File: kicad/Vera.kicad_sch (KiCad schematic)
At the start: 33 parts, among them Q1 AO3400 logic-level N-MOSFET, T1 Wurth 749010012A, T2 Wurth 749010012A, U1 TI AM62A7, U2 Microchip KSZ9477 7-port swit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, U3 TI MSPM0G3507, U4 TI ISOW1044BDFMR (isolated CA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, U5 Infineon SLB9670 TPM 2.0, Y1 25MHz crystal (2-pin symbol s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

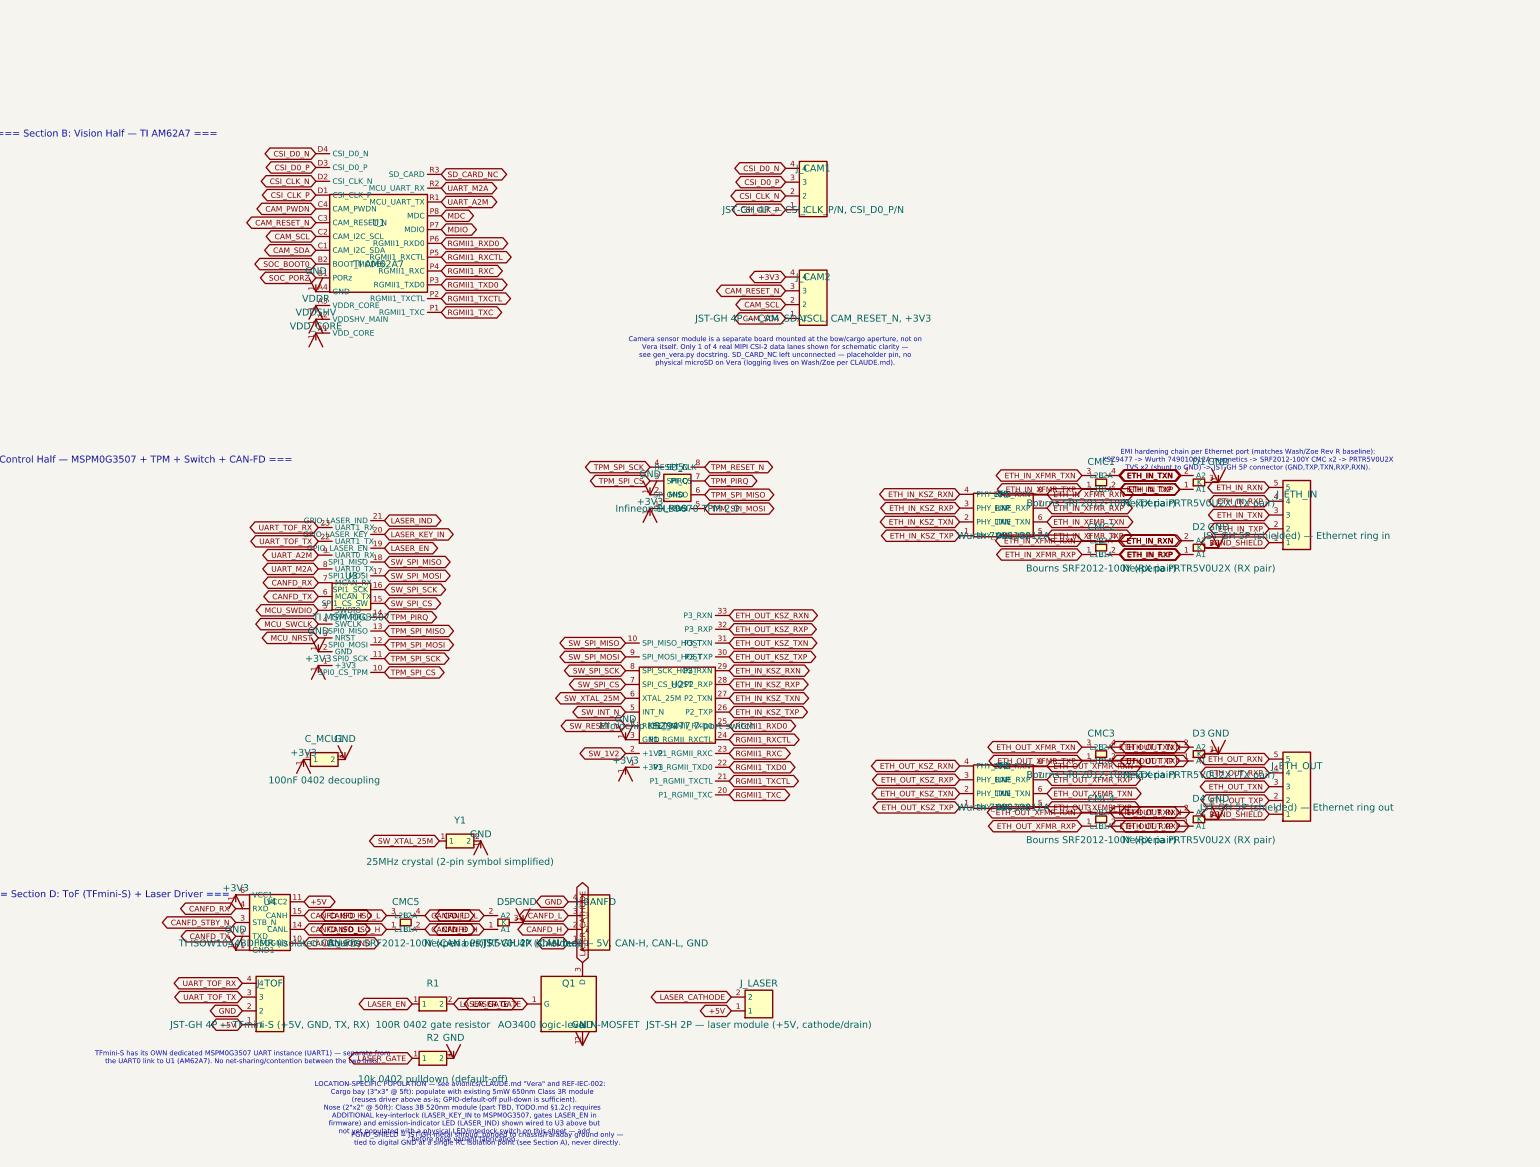
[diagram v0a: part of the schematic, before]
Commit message: Vera: add dual JST/direct-solder sensor interface (camera/ToF/laser) -- schematic
Section 4 of the readiness doc: each nose sensor aperture (camera/ToF/laser) gets
BOTH a JST connector AND a co-located direct-solder land on the SAME nets; populate
one per build (cargo=JST, nose=direct-solder aligned to the sensor mounting plate).

- gen_vera_ds_footprints.py -> Vera.pretty/{DS_Camera_9P,DS_ToF_4P,DS_Laser_2P}.
  kicad_mod: clean-room SMD pad-row lands (1.0mm pitch), pad<->signal order matches
  the JST group. Load in kicad-cli.
- gen_vera.py: adds SolderLand_09P/04P/02P symbols + J_CAM_DS / J_TOF_DS /
  J_LASER_DS instances on the exact JST nets (CSI/I2C/reset/+3V3/GND; +5V/GND/
  TOF_TX/RX; +5V/LASER_CATHODE), grid-aligned, with a populate-one-per-build note.
- fp-lib-table: register the project 'Vera' footprint lib (resolves the DS lands).

ERC 151->154 (+3 = the generic embedded-symbol lib ref that every symbol in this
generated schematic already carries; no connectivity defect -- DS pins join the JST
nets by global label). PCB placement (aligning lands to CAM_POS/TOF_POS/laser CL)
is the next step via a pcbnew script; final XY is a manual mechanical fit.

Co-Authored-By: Claude Opus 4.8 <noreply@anthropic.com>
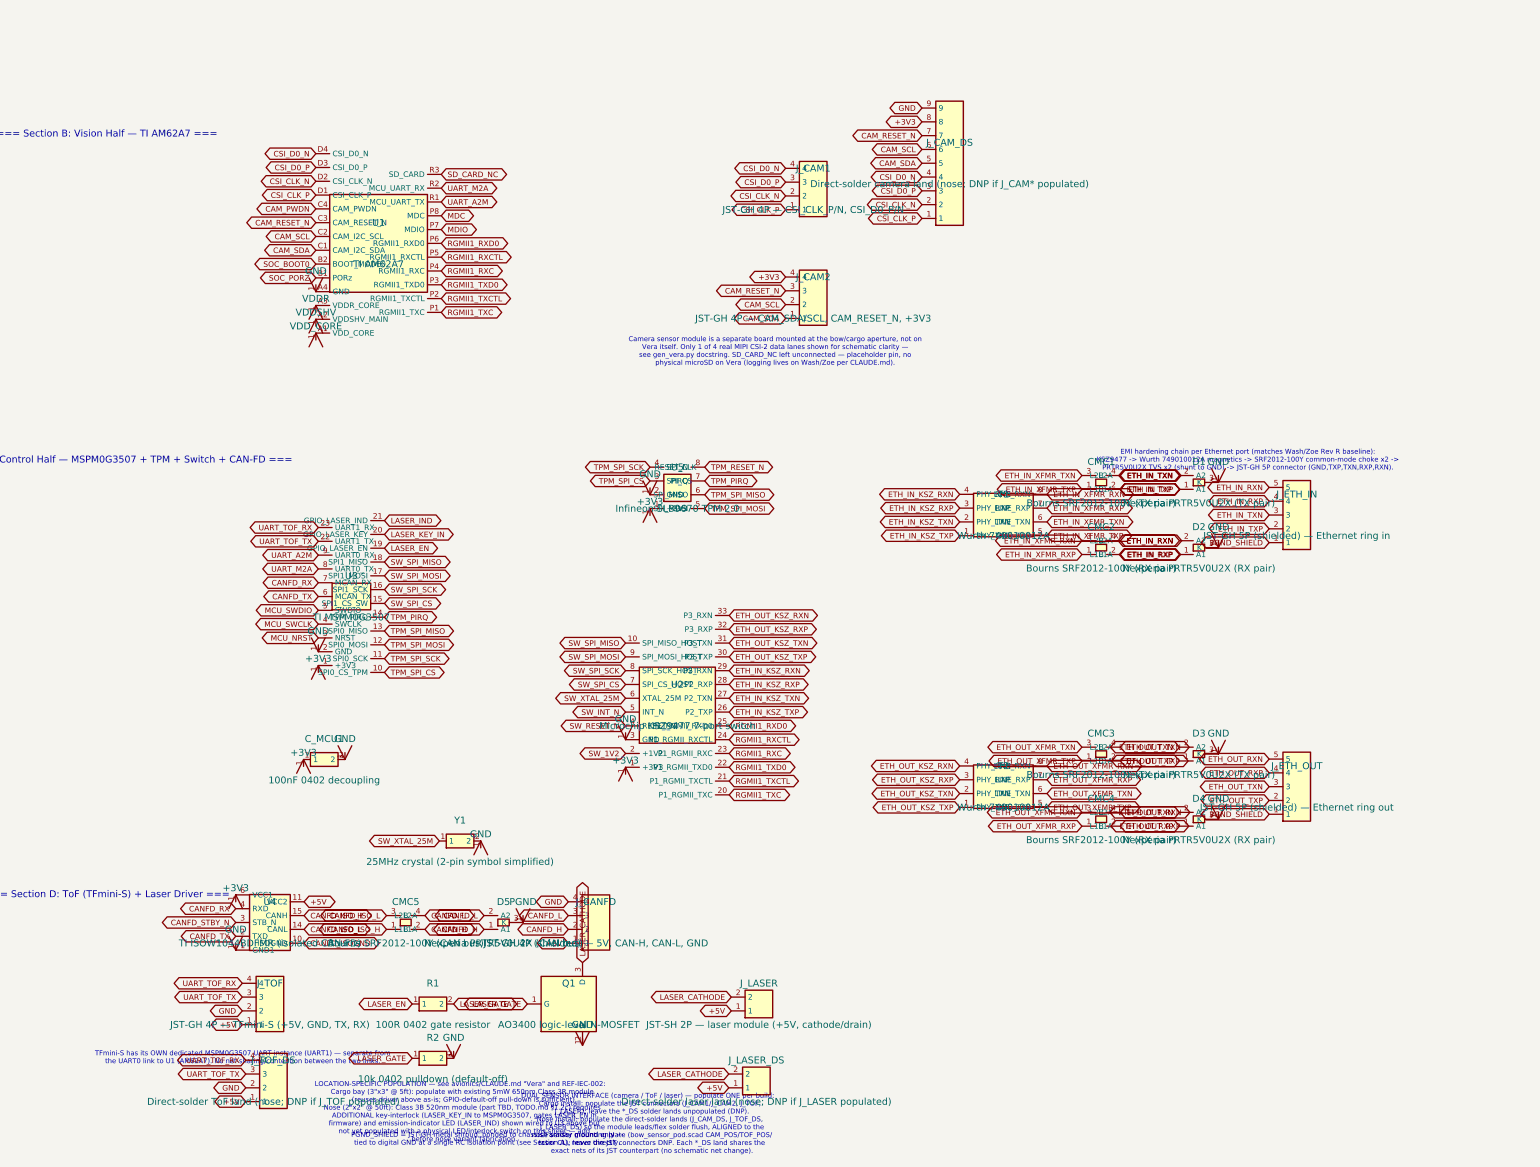
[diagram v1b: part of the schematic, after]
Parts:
- removed CMC1, CMC3: Bourns SRF2012-100Y (TX pair), symbol BOURNS_SRF2012_100Y
- removed CMC2, CMC4: Bourns SRF2012-100Y (RX pair), symbol BOURNS_SRF2012_100Y
- removed CMC5: Bourns SRF2012-100Y (CAN bus), symbol BOURNS_SRF2012_100Y
- added D2, D4: Nexperia PRTR5V0U2X (RX pair), symbol NEXPERIA_PRTR5V0U2X
- added J_CAM_DS: Direct-solder camera land (nose; DNP if J_CAM* po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, Vera:DS_Camera_9P, symbol SolderLand_09P
- added J_CANFD: JST-GH 4P (shielded) — 5V, CAN-H, CAN-L, GND, symbol Conn_JST_GH_04P
- added J_ETH_IN: JST-GH 5P (shielded) — Ethernet ring in, symbol Conn_JST_GH_05P
- added J_ETH_OUT: JST-GH 5P (shielded) — Ethernet ring out, symbol Conn_JST_GH_05P
- added J_LASER_DS: Direct-solder laser land (nose; DNP if J_LASER po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, Vera:DS_Laser_2P, symbol SolderLand_02P
- added J_TOF_DS: Direct-solder ToF land (nose; DNP if J_TOF popula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, Vera:DS_ToF_4P, symbol SolderLand_04P
- CMC1: renamed from D1; value Nexperia PRTR5V0U2X (TX pair) -> Bourns SRF2012-100Y (TX pair); symbol NEXPERIA_PRTR5V0U2X -> BOURNS_SRF2012_100Y
- CMC2: renamed from D2; value Nexperia PRTR5V0U2X (RX pair) -> Bourns SRF2012-100Y (RX pair); symbol NEXPERIA_PRTR5V0U2X -> BOURNS_SRF2012_100Y
- CMC3: renamed from D3; value Nexperia PRTR5V0U2X (TX pair) -> Bourns SRF2012-100Y (TX pair); symbol NEXPERIA_PRTR5V0U2X -> BOURNS_SRF2012_100Y
- CMC4: renamed from D4; value Nexperia PRTR5V0U2X (RX pair) -> Bourns SRF2012-100Y (RX pair); symbol NEXPERIA_PRTR5V0U2X -> BOURNS_SRF2012_100Y
- CMC5: renamed from J_CANFD; value JST-GH 4P (shielded) — 5V, CAN-H, CAN-L, GND -> Bourns SRF2012-100Y (CAN bus); symbol Conn_JST_GH_04P -> BOURNS_SRF2012_100Y
- D1: renamed from J_ETH_IN; value JST-GH 5P (shielded) — Ethernet ring in -> Nexperia PRTR5V0U2X (TX pair); symbol Conn_JST_GH_05P -> NEXPERIA_PRTR5V0U2X
- D3: renamed from J_ETH_OUT; value JST-GH 5P (shielded) — Ethernet ring out -> Nexperia PRTR5V0U2X (TX pair); symbol Conn_JST_GH_05P -> NEXPERIA_PRTR5V0U2X
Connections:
- net +3V3: now also J_CAM_DS.8
- net +5V: now also J_CANFD.1, J_LASER_DS.1, J_TOF_DS.1; no longer CMC5.1
- net CAM_RESET_N: now also J_CAM_DS.7
- net CAM_SCL: now also J_CAM_DS.6
- net CAM_SDA: now also J_CAM_DS.5
- net CANFD_H: now also J_CANFD.2
- net CANFD_ISO_H: now also CMC5.1 (L1A)
- net CANFD_ISO_L: now also CMC5.3 (L2A)
- net CANFD_L: now also CMC5.4 (L2B), J_CANFD.3; no longer CMC5.3
- net CSI_CLK_N: now also J_CAM_DS.2
- net CSI_CLK_P: now also J_CAM_DS.1
- net CSI_D0_N: now also J_CAM_DS.4
- net CSI_D0_P: now also J_CAM_DS.3
- net ETH_IN_RXN: now also CMC2.4 (L2B), D2.2 (A2), J_ETH_IN.5; no longer CMC2.2 (A2), D1.5
- net ETH_IN_RXP: now also CMC2.2 (L1B), D2.1 (A1), J_ETH_IN.4; no longer CMC2.1 (A1), D1.4
- net ETH_IN_TXN: now also CMC1.4 (L2B), D1.2 (A2), J_ETH_IN.3; no longer CMC1.2 (A2), D1.3
- net ETH_IN_TXP: now also CMC1.2 (L1B), D1.1 (A1), J_ETH_IN.2; no longer CMC1.1 (A1), D1.2
- net ETH_IN_XFMR_RXN: now also CMC2.3 (L2A)
- net ETH_IN_XFMR_RXP: now also CMC2.1 (L1A)
- net ETH_IN_XFMR_TXN: now also CMC1.3 (L2A)
- net ETH_IN_XFMR_TXP: now also CMC1.1 (L1A)
- net ETH_OUT_RXN: now also CMC4.4 (L2B), D4.2 (A2), J_ETH_OUT.5; no longer CMC4.2 (A2), D3.5
- net ETH_OUT_RXP: now also CMC4.2 (L1B), D4.1 (A1), J_ETH_OUT.4; no longer CMC4.1 (A1), D3.4
- net ETH_OUT_TXN: now also CMC3.4 (L2B), D3.2 (A2), J_ETH_OUT.3; no longer CMC3.2 (A2), D3.3
- net ETH_OUT_TXP: now also CMC3.2 (L1B), D3.1 (A1), J_ETH_OUT.2; no longer CMC3.1 (A1), D3.2
- net ETH_OUT_XFMR_RXN: now also CMC4.3 (L2A)
- net ETH_OUT_XFMR_RXP: now also CMC4.1 (L1A)
- net ETH_OUT_XFMR_TXN: now also CMC3.3 (L2A)
- net ETH_OUT_XFMR_TXP: now also CMC3.1 (L1A)
- net GND: now also D1.3 (K), D3.3 (K), D2.3 (K), D4.3 (K), J_CAM_DS.9, J_CANFD.4, J_TOF_DS.2; no longer CMC1.3 (K), CMC2.3 (K), CMC3.3 (K), CMC4.3 (K), CMC5.4
- net LASER_CATHODE: now also J_LASER_DS.2
- net PGND_SHIELD: now also J_ETH_IN.1, J_ETH_OUT.1; no longer D1.1, D3.1
- net UART_TOF_RX: now also J_TOF_DS.4
- net UART_TOF_TX: now also J_TOF_DS.3
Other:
- note added: "DUAL SENSOR INTERFACE (camera / ToF / laser) — populate ONE per build: Cargo install: populate the JST connectors (J_CAM1/J_CAM2, J_TOF, J_LASER); leave the *_DS solder lands unpopulated (DNP). Nose install: populate the direct-solder lands (J_CAM_DS, J_TOF_DS, J_LASER_DS) so the module leads/flex solder flush, ALIGNED to the nose sensor mounting plate (bow_sensor_pod.scad CAM_POS/TOF_POS/ laser 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"
- note added: "EMI hardening chain per Ethernet port (matches Wash/Zoe Rev R baseline): KSZ9477 -> Wurth 749010012A magnetics -> SRF2012-100Y common-mode choke x2 -> PRTR5V0U2X TVS x2 (shunt to GND) -> JST-GH 5P connector (GND,TXP,TXN,RXP,RXN)."
- note removed: "EMI hardening chain per Ethernet port (matches Wash/Zoe Rev R baseline): KSZ9477 -> Wurth 749010012A magnetics -> SRF2012-100Y CMC x2 -> PRTR5V0U2X TVS x2 (shunt to GND) -> JST-GH 5P connector (GND,TXP,TXN,RXP,RXN)."
- moved on the sheet: CMC5
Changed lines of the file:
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@@
     (effects (font (size 0.90 0.90)))
 )
+  (symbol (lib_id "SolderLand_09P") (at 165.10 95.25 0)
+    (unit 1) (exclude_from_sim no) (in_bom yes) (on_board yes) (dnp no)
+    (property "Reference" "J_CAM_DS" (at 165.10 91.44 0)
+      (effects (font (size 1.27 1.27))))
+    (property "Value" "Direct-solder camera land (nose; DNP if J_CAM* populated)" (at 165.10 99.06 0)
+      (effects (font (size 1.27 1.27))))
+    (property "Footprint" "Vera:DS_Camera_9P" (at 0 0 0)
+      (effects (font (size 1.27 1.27)) (hide yes)))
+    (property "Datasheet" "" (at 0 0 0)
+      (effects (font (size 1.27 1.27)) (hide yes)))
+  )
+  (global_label "CSI_CLK_P" (shape bidirectional) (at 160.02 105.41 180)
+    (effects (font (size 1.016 1.016)))
+    (property "Intersheet References" "${INTERSHEET_REFS}" (at 160.02 105.41 0)
+      (effects (font (size 1.016 1.016)) (hide yes))))
+  (global_label "CSI_CLK_N" (shape bidirectional) (at 160.02 102.87 180)
+    (effects (font (size 1.016 1.016)))
+    (property "Intersheet References" "${INTERSHEET_REFS}" (at 160.02 102.87 0)
+      (effects (font (size 1.016 1.016)) (hide yes))))
+  (global_label "CSI_D0_P" (shape bidirectional) (at 160.02 100.33 180)
+    (effects (font (size 1.016 1.016)))
+    (property "Intersheet References" "${INTERSHEET_REFS}" (at 160.02 100.33 0)
+      (effects (font (size 1.016 1.016)) (hide yes))))
+  (global_label "CSI_D0_N" (shape bidirectional) (at 160.02 97.79 180)
+    (effects (font (size 1.016 1.016)))
+    (property "Intersheet References" "${INTERSHEET_REFS}" (at 160.02 97.79 0)
+      (effects (font (size 1.016 1.016)) (hide yes))))
+  (global_label "CAM_SDA" (shape bidirectional) (at 160.02 95.25 180)
+    (effects (font (size 1.016 1.016)))
+    (property "Intersheet References" "${INTERSHEET_REFS}" (at 160.02 95.25 0)
+      (effects (font (size 1.016 1.016)) (hide yes))))
+  (global_label "CAM_SCL" (shape bidirectional) (at 160.02 92.71 180)
+    (effects (font (size 1.016 1.016)))
+    (property "Intersheet References" "${INTERSHEET_REFS}" (at 160.02 92.71 0)
+      (effects (font (size 1.016 1.016)) (hide yes))))
+  (global_label "CAM_RESET_N" (shape bidirectional) (at 160.02 90.17 180)
+    (effects (font (size 1.016 1.016)))
+    (property "Intersheet References" "${INTERSHEET_REFS}" (at 160.02 90.17 0)
+      (effects (font (size 1.016 1.016)) (hide yes))))
+  (global_label "+3V3" (shape bidirectional) (at 160.02 87.63 180)
+    (effects (font (size 1.016 1.016)))
+    (property "Intersheet References" "${INTERSHEET_REFS}" (at 160.02 87.63 0)
+      (effects (font (size 1.016 1.016)) (hide yes))))
+  (global_label "GND" (shape bidirectional) (at 160.02 85.09 180)
+    (effects (font (size 1.016 1.016)))
+    (property "Intersheet References" "${INTERSHEET_REFS}" (at 160.02 85.09 0)
+      (effects (font (size 1.016 1.016)) (hide yes))))
   (text "=== Section C: Control Half — MSPM0G3507 + TPM + Switch + CAN-FD ===" (at 10.00 150.00 0)
     (effects (font (size 1.27 1.27)))
@@
     (pin "1")
   )
-  (text "EMI hardening chain per Ethernet port (matches Wash/Zoe Rev R baseline):\nKSZ9477 -> Wurth 749010012A magnetics -> SRF2012-100Y CMC x2 -> PRTR5V0U2X\nTVS x2 (shunt to GND) -> JST-GH 5P connector (GND,TXP,TXN,RXP,RXN)." (at 220.00 150.00 0)
+  (text "EMI hardening chain per Ethernet port (matches Wash/Zoe Rev R baseline):\nKSZ9477 -> Wurth 749010012A magnetics -> SRF2012-100Y common-mode choke x2 ->\nPRTR5V0U2X TVS x2 (shunt to GND) -> JST-GH 5P connector (GND,TXP,TXN,RXP,RXN)." (at 220.00 150.00 0)
     (effects (font (size 0.90 0.90)))
 )
@@
     (effects (font (size 0.90 0.90)))
 )
+  (symbol (lib_id "SolderLand_04P") (at 40.64 264.16 0)
+    (unit 1) (exclude_from_sim no) (in_bom yes) (on_board yes) (dnp no)
+    (property "Reference" "J_TOF_DS" (at 40.64 260.35 0)
+      (effects (font (size 1.27 1.27))))
+    (property "Value" "Direct-solder ToF land (nose; DNP if J_TOF populated)" (at 40.64 267.97 0)
+      (effects (font (size 1.27 1.27))))
+    (property "Footprint" "Vera:DS_ToF_4P" (at 0 0 0)
+      (effects (font (size 1.27 1.27)) (hide yes)))
+    (property "Datasheet" "" (at 0 0 0)
+      (effects (font (size 1.27 1.27)) (hide yes)))
+  )
+  (global_label "+5V" (shape bidirectional) (at 35.56 267.97 180)
+    (effects (font (size 1.016 1.016)))
+    (property "Intersheet References" "${INTERSHEET_REFS}" (at 35.56 267.97 0)
+      (effects (font (size 1.016 1.016)) (hide yes))))
+  (global_label "GND" (shape bidirectional) (at 35.56 265.43 180)
+    (effects (font (size 1.016 1.016)))
+    (property "Intersheet References" "${INTERSHEET_REFS}" (at 35.56 265.43 0)
+      (effects (font (size 1.016 1.016)) (hide yes))))
+  (global_label "UART_TOF_TX" (shape bidirectional) (at 35.56 262.89 180)
+    (effects (font (size 1.016 1.016)))
+    (property "Intersheet References" "${INTERSHEET_REFS}" (at 35.56 262.89 0)
+      (effects (font (size 1.016 1.016)) (hide yes))))
+  (global_label "UART_TOF_RX" (shape bidirectional) (at 35.56 260.35 180)
+    (effects (font (size 1.016 1.016)))
+    (property "Intersheet References" "${INTERSHEET_REFS}" (at 35.56 260.35 0)
+      (effects (font (size 1.016 1.016)) (hide yes))))
   (symbol (lib_id "AO3400") (at 95.00 250.00 0)
     (unit 1) (exclude_from_sim no) (in_bom yes) (on_board yes) (dnp no)
@@
     (property "Intersheet References" "${INTERSHEET_REFS}" (at 124.92 248.73 0)
       (effects (font (size 1.016 1.016)) (hide yes))))
+  (symbol (lib_id "SolderLand_02P") (at 129.54 264.16 0)
+    (unit 1) (exclude_from_sim no) (in_bom yes) (on_board yes) (dnp no)
+    (property "Reference" "J_LASER_DS" (at 129.54 260.35 0)
+      (effects (font (size 1.27 1.27))))
+    (property "Value" "Direct-solder laser land (nose; DNP if J_LASER populated)" (at 129.54 267.97 0)
+      (effects (font (size 1.27 1.27))))
+    (property "Footprint" "Vera:DS_Laser_2P" (at 0 0 0)
+      (effects (font (size 1.27 1.27)) (hide yes)))
+    (property "Datasheet" "" (at 0 0 0)
+      (effects (font (size 1.27 1.27)) (hide yes)))
+  )
+  (global_label "+5V" (shape bidirectional) (at 124.46 265.43 180)
+    (effects (font (size 1.016 1.016)))
+    (property "Intersheet References" "${INTERSHEET_REFS}" (at 124.46 265.43 0)
+      (effects (font (size 1.016 1.016)) (hide yes))))
+  (global_label "LASER_CATHODE" (shape bidirectional) (at 124.46 262.89 180)
+    (effects (font (size 1.016 1.016)))
+    (property "Intersheet References" "${INTERSHEET_REFS}" (at 124.46 262.89 0)
+      (effects (font (size 1.016 1.016)) (hide yes))))
+  (text "DUAL SENSOR INTERFACE (camera / ToF / laser) — populate ONE per build:\n  Cargo install: populate the JST connectors (J_CAM1/J_CAM2, J_TOF,\n    J_LASER); leave the *_DS solder lands unpopulated (DNP).\n  Nose install: populate the direct-solder lands (J_CAM_DS, J_TOF_DS,\n    J_LASER_DS) so the module leads/flex solder flush, ALIGNED to the\n    nose sensor mounting plate (bow_sensor_pod.scad CAM_POS/TOF_POS/\n    laser CL); leave the JST connectors DNP. Each *_DS land shares the\n    exact nets of its JST counterpart (no schematic net change)." (at 109.54 272.16 0)
+    (effects (font (size 0.90 0.90)))
+)
   (text "LOCATION-SPECIFIC POPULATION — see avionics/CLAUDE.md \"Vera\" and REF-IEC-002:\n  Cargo bay (3\"x3\" @ 5ft): populate with existing 5mW 650nm Class 3R module\n    (reuses driver above as-is; GPIO-default-off pull-down is sufficient).\n  Nose (2\"x2\" @ 50ft): Class 3B 520nm module (part TBD, TODO.md §1.2c) requires\n    ADDITIONAL key-interlock (LASER_KEY_IN to MSPM0G3507, gates LASER_EN in\n    firmware) and emission-indicator LED (LASER_IND) shown wired to U3 above but\n    not yet populated with a physical LED/interlock switch on this sheet — add\n    before nose variant fabrication." (at 75.00 270.00 0)
     (effects (font (size 0.90 0.90)))
